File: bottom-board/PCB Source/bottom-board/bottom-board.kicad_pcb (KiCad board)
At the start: 4 copper layers, 194 x 94 mm, 308 parts, among them J1 AS0A823-H4SB-7H, P1 USB_B, P10 JACK_TRS_6PINS, P11 JACK_TRS_6PINS, P12 JACK_TRS_6PINS, P13 RJ45, P14 AudioJack3, P2 USB_A, P3 BARREL_JACK, P5 HMI_DATA, P6 AudioJack3, P7 AudioJack3, P8 SERIAL_DEBUG, P9 JACK_TRS_6PINS, Q1 2N7002, Q10 MMBFJ110, Q12 2N7002, Q13 2N7002, Q2 2N7002, Q3 MMBFJ110, Q4 MMBFJ110, Q5 MMBFJ110, Q6 MMBFJ110, Q7 2N7002, Q8 2N7002, Q9 MMBFJ110, U1 TS2596, U10 TPS2001DDBVR, U11 6N137S, U12 ISL83491, U13 AP2120N-3.3, U2 TL750M10CKVURG3, U3 CS4265, U4 AT24CS08-STUM, U5 LM4562, U6 OPA1678, U7 OPA1678, U8 LM4811, U9 LD1117S50TR_SOT223, X1 24.576MHz

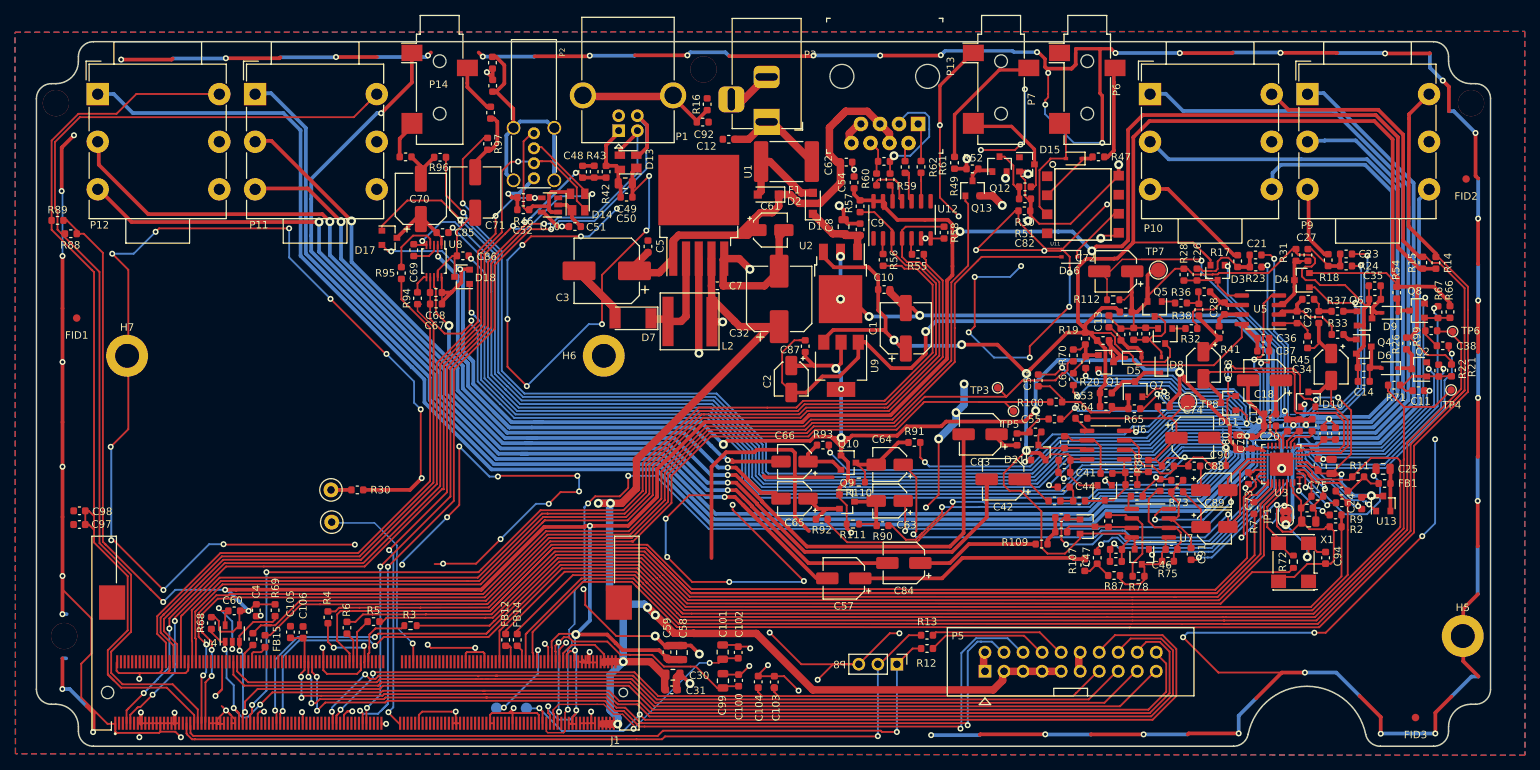
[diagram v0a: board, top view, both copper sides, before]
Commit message: update PCB, add noisefix components
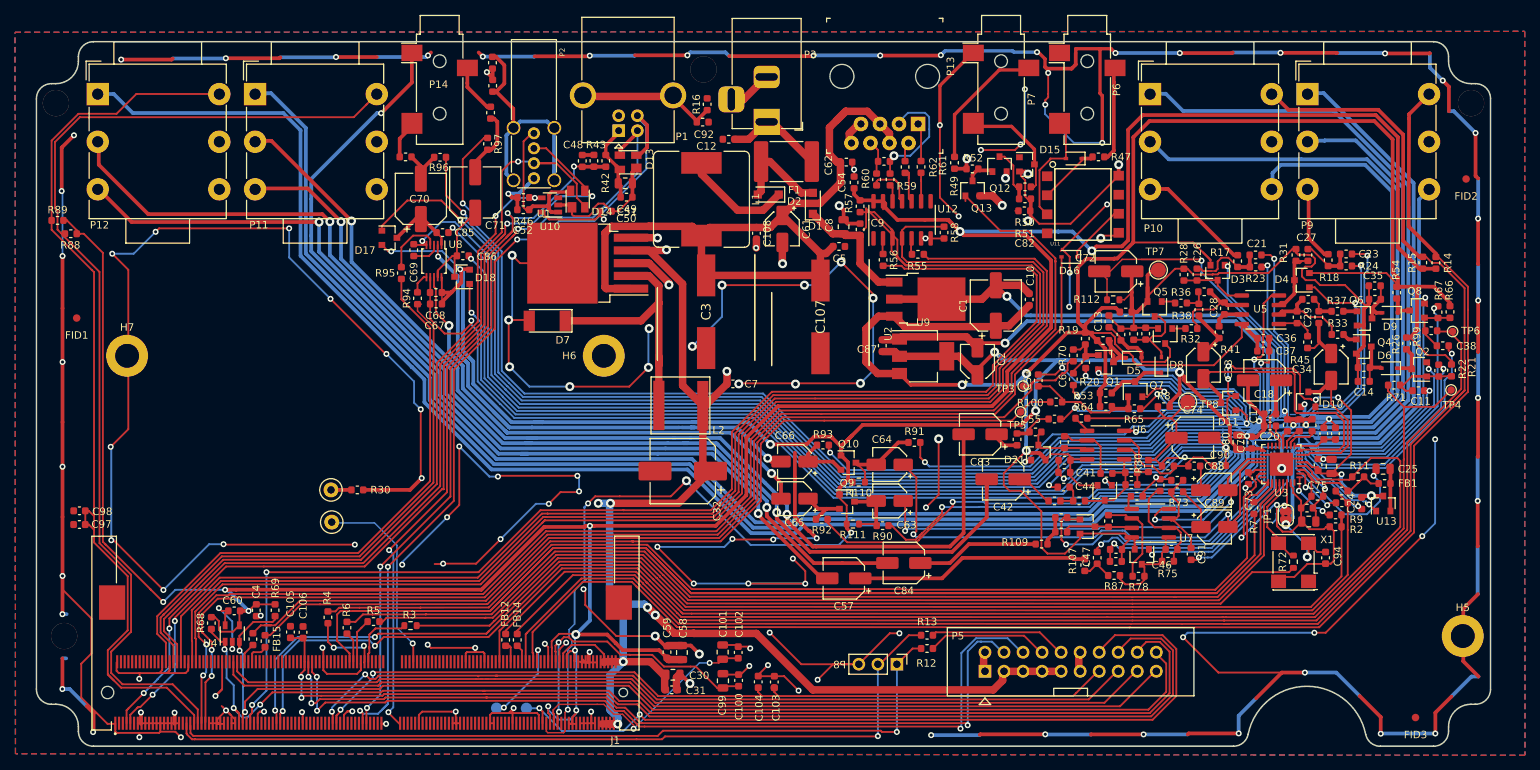
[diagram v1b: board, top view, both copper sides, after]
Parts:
- added C107: 1000uF, Uno:CAPAE1300X1400N, F.Cu at (163.5, 78.2)
- added C108: 1nF, Capacitor_SMD:C_0603_1608Metric, F.Cu at (155.0, 67.0)
- added L1: 1mH, Inductor_SMD:L_Bourns_SRR1260, F.Cu at (147.6, 62.5)
- C101, C30, C58, C99: value 10uF -> 22uF
- C3: value 470uF -> 1000uF; footprint Capacitor_SMD:CP_Elec_8x10.5 -> Uno:CAPAE1300X1400N
- moved C32 26.3 mm to (145.1, 98.7), turned to 180 degrees
- moved C5 25.5 mm to (166.0, 68.8), turned to 0 degrees
- moved C2 25.0 mm to (184.5, 84.1), turned to 90 degrees
- moved C10 19.4 mm to (191.4, 75.8), turned to 90 degrees
- moved U1 16.1 mm to (132.5, 71.0), turned to 180 degrees
- moved C3 14.3 mm to (148.3, 77.5), turned to 270 degrees
- moved C7 13.3 mm to (151.8, 87.1)
- moved C1 12.4 mm to (186.9, 76.6)
- moved U2 11.6 mm to (177.6, 75.8), turned to 0 degrees
- moved D7 11.5 mm to (127.1, 78.7)
- moved L2 11.3 mm to (147.0, 90.0)
- moved U9 11.0 mm to (177.2, 83.4), turned to 0 degrees
- moved C87 10.3 mm to (171.8, 82.0)
- moved C51 4.59 mm to (134.9, 64.1)
- moved TP3 3.42 mm to (190.6, 87.4)
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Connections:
- D2 pad 1: +12V -> Net-(D2-Pad1)
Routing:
- net GNDD: track 1433.7 -> 1355.0 mm, vias 141 -> 144
- net GNDA: track 3565.9 -> 3507.9 mm, vias 69 -> 66
- net CHAIN_UART_RE: track 150.0 -> 194.3 mm
- net +12V: track 64.6 -> 102.0 mm
- net CHAIN_UART_DE: track 148.7 -> 178.9 mm
- net CHAIN_UART_RX: track 142.0 -> 171.9 mm
- net CHAIN_UART_TX: track 137.5 -> 166.8 mm
- net +3V3: track 392.3 -> 416.6 mm
- net MIDI_UART_TX: track 155.0 -> 177.2 mm
- net Net-(D7-Pad1): track 12.6 -> 34.8 mm
- net Net-(D2-Pad1): track 0.00 -> 14.8 mm
- net +5V: track 209.2 -> 219.3 mm, vias 12 -> 13
- net IN2_GC2: track 132.9 -> 122.8 mm
- net Net-(C8-Pad1): track 9.83 -> 16.8 mm
- net USB_DEV_DET: track 99.1 -> 95.2 mm
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
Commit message: update fabrication data
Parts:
- moved R3 1.67 mm to (107.1, 119.3)
- moved R69 0.83 mm to (90.2, 117.9)
- moved C4 0.72 mm to (88.6, 117.9)
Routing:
- net GNDD: track 1355.0 -> 1527.6 mm, vias 144 -> 151
- net CODEC_I2S_SDOUT: track 273.6 -> 238.8 mm
- net +3V3: track 416.6 -> 411.0 mm
- net (no net): track 0.00 -> 4.77 mm
- net +10V: track 321.9 -> 317.2 mm
- net IN2_DETECT: track 215.6 -> 211.0 mm
- net Net-(C66-Pad2): track 71.4 -> 67.2 mm
- net +5V: track 219.3 -> 215.3 mm, vias 13 -> 12
- net CODEC_I2S_MCLK: track 9.03 -> 5.03 mm
- net +5VA: track 357.3 -> 361.0 mm
- net Net-(C65-Pad2): track 68.0 -> 71.2 mm
- net Net-(C83-Pad2): track 138.1 -> 135.9 mm
- net Net-(C42-Pad2): track 133.1 -> 130.9 mm
- net Net-(R3-Pad1): track 125.1 -> 126.8 mm
- net PM_LEDS_SDA: track 152.8 -> 154.3 mm
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
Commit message: clean bottomboard, upload fabrication
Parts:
- C20, C37, C41, C45, C67, C69, C96: footprint Capacitor_SMD:C_0603_1608Metric -> Capacitor_SMD:C_0805_2012Metric
- moved C57 16.2 mm to (182.6, 110.3)
- moved C84 14.8 mm to (188.6, 105.9)
- moved R87 6.90 mm to (195.9, 111.5), turned to 0 degrees
- moved R78 2.61 mm to (205.6, 110.2), turned to 90 degrees
- moved D20 2.12 mm to (208.5, 110.1)
- moved R75 2.03 mm to (211.9, 110.8)
- moved C46 1.55 mm to (211.9, 109.2)
- moved C91 1.38 mm to (214.3, 109.8)
- moved R107 1.36 mm to (198.3, 110.0)
- moved C17 0.66 mm to (223.5, 90.4)
- moved R95 0.64 mm to (107.0, 72.2)
- moved C45 0.48 mm to (202.6, 111.2)
- moved C20 0.43 mm to (223.2, 92.4)
- moved C47 0.40 mm to (200.0, 110.4)
- moved C67 0.33 mm to (112.3, 76.8)
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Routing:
- net CODEC_I2S_SDOUT: track 238.8 -> 158.9 mm
- net GNDD: track 1527.6 -> 1566.4 mm, vias 151 -> 152
- net OUTPUT_BIAS: track 43.3 -> 66.1 mm
- net +5V: track 215.3 -> 235.9 mm, vias 12 -> 14
- net Net-(C57-Pad1): track 31.0 -> 14.1 mm
- net Net-(C57-Pad2): track 124.9 -> 140.4 mm
- net Net-(C84-Pad2): track 135.7 -> 151.2 mm
- net Net-(C84-Pad1): track 17.0 -> 3.42 mm
- net +10V: track 317.2 -> 327.0 mm
- net Net-(C22-Pad1): track 10.7 -> 19.9 mm
- net Net-(D22-Pad3): track 8.83 -> 17.8 mm
- net Net-(C46-Pad1): track 12.8 -> 20.9 mm
- net (no net): track 4.77 -> 0.00 mm
- net +3V3: track 411.0 -> 414.4 mm
- net Net-(C38-Pad1): track 8.37 -> 11.7 mm
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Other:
- board text added: "MOD Devices GmbH http://moddevices.com [MDW-ELE-001] MOD Dwarf - Main Board Rev.: MDW-PX30-V1.05 Date: 2021.10.08"
- board text removed: "MOD Devices GmbH http://moddevices.com [MDW-ELE-001] MOD Dwarf - Main Board Rev.: MDW-PX30-V1.05 Date: 2021.XXXX"

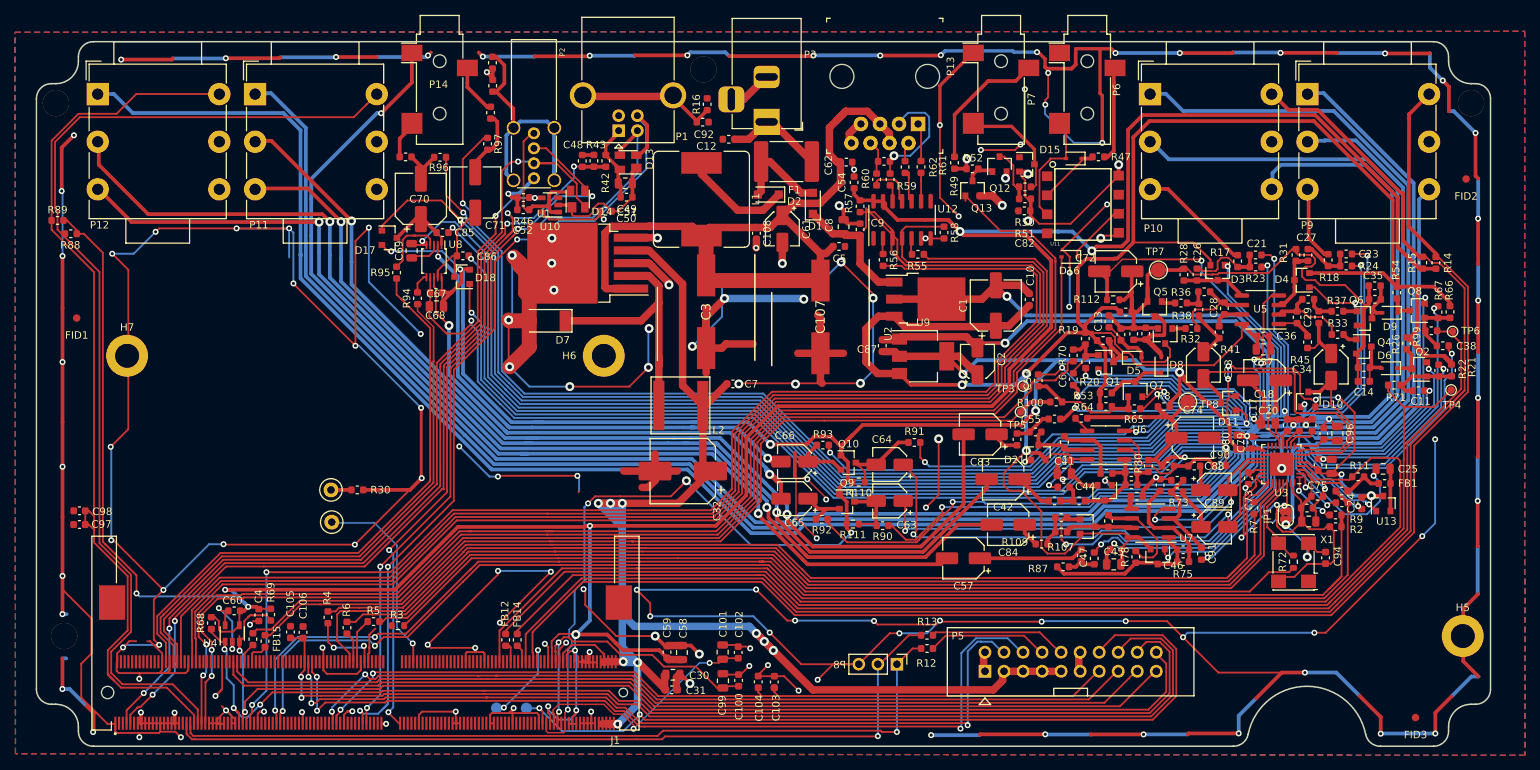
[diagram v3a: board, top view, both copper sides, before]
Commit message: change input bias 5->6V, reduce harmonics
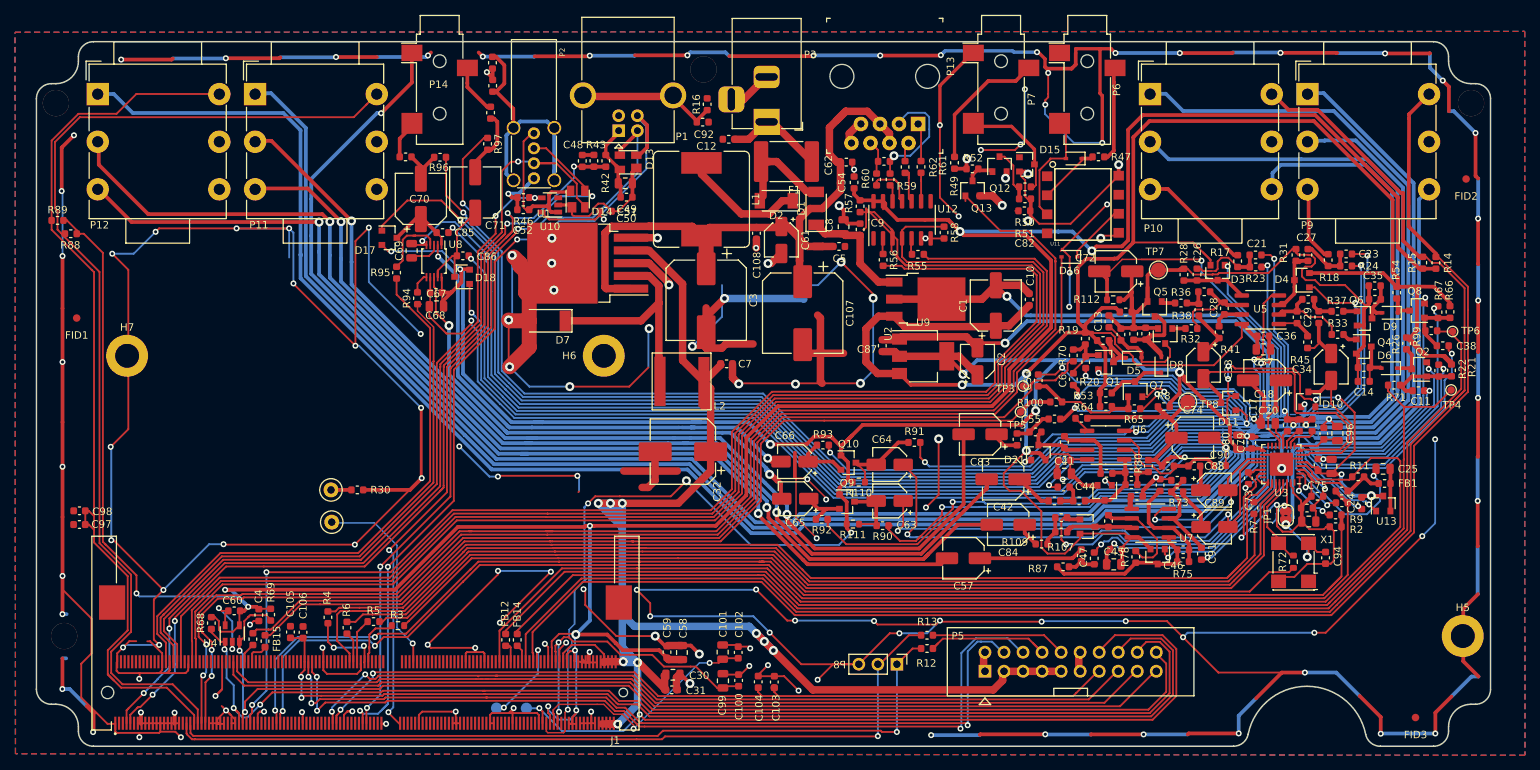
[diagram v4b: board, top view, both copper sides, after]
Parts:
- C107, C3: footprint Uno:CAPAE1300X1400N -> Capacitor_SMD:CP_Elec_10x10.5
- D1, D2: footprint Diode_SMD:D_SOD-123F -> Diode_SMD:D_SOD-128
- moved L2 3.20 mm to (147.2, 86.8)
- moved C7 2.81 mm to (151.0, 84.4)
- moved C32 2.59 mm to (145.2, 96.1)
- moved C107 2.42 mm to (161.1, 77.7)
- moved C3 1.53 mm to (148.3, 75.9)
- moved C61 1.49 mm to (158.3, 67.9)
- moved D2 1.35 mm to (157.6, 62.6)
- moved D1 0.80 mm to (162.9, 63.7)
- moved C65 0.10 mm to (160.2, 102.4)
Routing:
- net +12V: track 102.0 -> 92.6 mm
- net Net-(D7-Pad1): track 34.8 -> 29.4 mm
- net GNDA: track 3505.7 -> 3508.8 mm
- net Net-(P5-Pad8): track 16.0 -> 18.5 mm
- net CODEC_I2S_MCLK: track 5.03 -> 7.36 mm
- net Net-(D2-Pad1): track 14.8 -> 16.6 mm
- net Net-(D1-Pad2): track 13.2 -> 15.0 mm
- net CODEC_DAC_A: track 58.8 -> 60.3 mm
- net CODEC_DAC_B: track 67.7 -> 69.0 mm
- net Net-(C8-Pad1): track 16.8 -> 15.8 mm
- net +5V: track 235.9 -> 235.1 mm
- net Net-(C84-Pad2): track 151.2 -> 151.9 mm
- net GNDD: track 1566.4 -> 1565.8 mm, vias 152 -> 150

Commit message: update fabrication data
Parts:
- moved C91 0.40 mm to (214.4, 110.1)
- renumbered Power1 to Power, Reset1 to Reset
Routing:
- net GNDA: track 3508.8 -> 3509.9 mm
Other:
- board text added: "MOD Devices GmbH http://moddevices.com [MDW-ELE-001] MOD Dwarf - Main Board Rev.: MDW-PX30-V1.05 Date: 2021.11.10"
- board text removed: "MOD Devices GmbH http://moddevices.com [MDW-ELE-001] MOD Dwarf - Main Board Rev.: MDW-PX30-V1.05 Date: 2021.10.08"

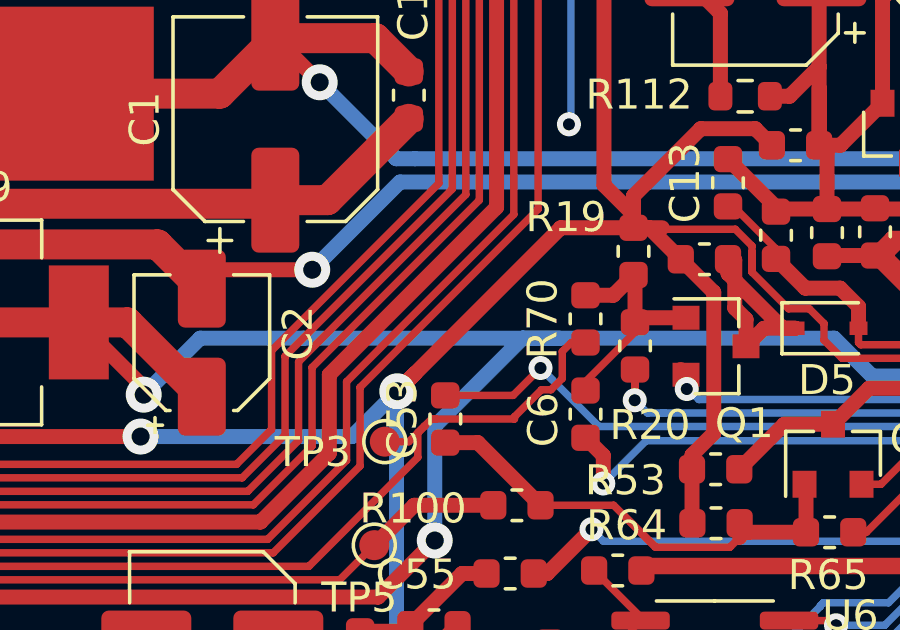
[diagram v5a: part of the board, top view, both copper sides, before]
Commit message: correct MPN R112, U6 and U7
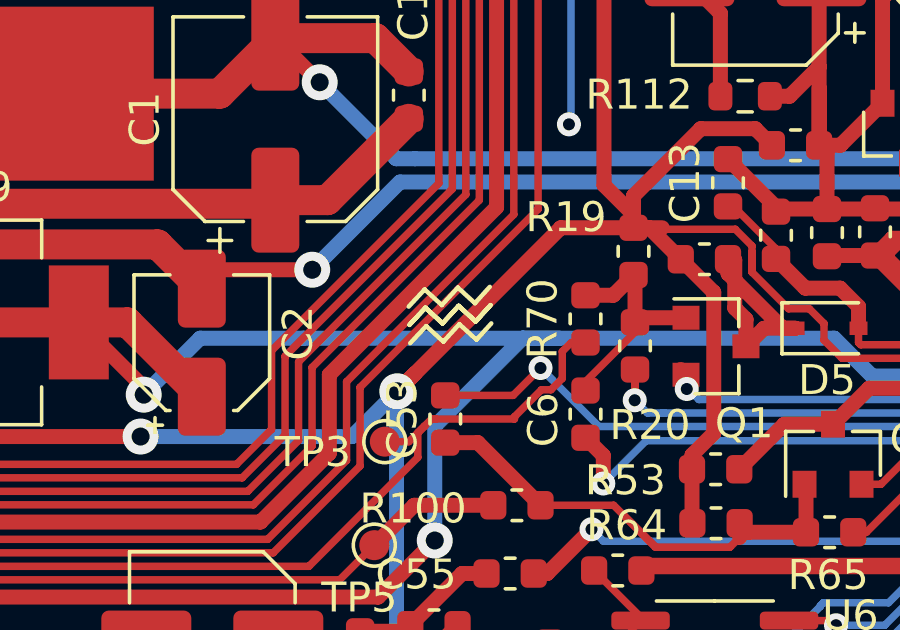
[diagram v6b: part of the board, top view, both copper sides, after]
